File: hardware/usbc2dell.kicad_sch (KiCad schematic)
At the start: 20 parts, among them J1 USB_C_Receptacle_PowerOnly_6P, J2 DELL_Charger, Q1 Q_NMOS_GDS, Q2 Q_NPN_BEC, SW1 SW_DIP_x04, U1 ATtiny1616-M, U2 FUSB302BMPX, U3 L7805

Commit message: add caps
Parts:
- added C1, C3: 100n, Capacitor_SMD:C_0603_1608Metric, symbol Device:C
- added C2, C4: 1u, Capacitor_SMD:C_0603_1608Metric, symbol Device:C
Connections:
- net GND: now also C1.2, C2.2, C3.2, C4.2
- net VBUS: now also C1.1, C2.1
- net VCC: now also C3.1, C4.1
- net Vout: now reaches J2.3 (Pin_3), Q1.3 (S)

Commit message: prod?
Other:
- note added: "LED"
- note added: "caps"
- note added: "support / protection"
- company: (none) -> H3
- title: (none) -> USB Type-C to legacy Charging-Connector Adapter
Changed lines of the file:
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@@
 	(generator_version "9.0")
 	(paper "A4")
+	(title_block
+		(title "USB Type-C to legacy Charging-Connector Adapter")
+		(date "2025")
+		(rev "v0.1")
+		(company "H3")
+	)
 	(rectangle
 		(start 101.6 101.6)
@@
 		)
 	)
+	(text "caps"
+		(exclude_from_sim no)
+		(at 87.63 147.32 0)
+		(effects
+			(font
+				(size 1.27 1.27)
+			)
+			(justify right top)
+		)
+	)
 	(text "Software:\n- Negotiate PD profile up to 20V\n- Emulate DELLCHG EEPROM with values from PD profile\n- Enable power output"
 		(exclude_from_sim no)
@@
 		)
 	)
+	(text "LED"
+		(exclude_from_sim no)
+		(at 87.63 102.87 0)
+		(effects
+			(font
+				(size 1.27 1.27)
+			)
+			(justify right top)
+		)
+	)
+	(text "support / protection"
+		(exclude_from_sim no)
+		(at 189.23 102.87 0)
+		(effects
+			(font
+				(size 1.27 1.27)
+			)
+			(justify right top)
+		)
+	)

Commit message: parts sel
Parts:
- C1, C3: LCSC (none) -> C14663
- C2, C4: LCSC (none) -> C15849
- D1: value LED_RGB -> TC5050RGBF08-3CJH-AF53A; LCSC (none) -> C784540
- J1: value USB_C_Receptacle_PowerOnly_6P -> TYPE-C-31-M-17; LCSC (none) -> C283540
- Q1: value Q_NMOS_GDS -> MDD50N03D; LCSC (none) -> C5357578
- Q2: value Q_NPN_BEC -> MMBT5551; LCSC (none) -> C2145
- R1: value 10k -> 4k7; LCSC (none) -> C23162
- R2, R3, R4: LCSC (none) -> C23162
- R5: LCSC (none) -> C22775
- TP1, TP2, TP3: now left out of the parts list
- U2: LCSC (none) -> C442699
- U3: LCSC (none) -> C86206
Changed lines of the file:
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@@
+			)
+		)
+		(property "LCSC" "C442699"
+			(at 99.06 68.58 0)
+			(effects
+				(font
+					(size 1.27 1.27)
+				)
+				(hide yes)
 			)
 		)
@@
 			)
 		)
+		(property "LCSC" "C14663"
+			(at 57.15 158.75 0)
+			(effects
+				(font
+					(size 1.27 1.27)
+				)
+				(hide yes)
+			)
+		)
 		(pin "1"
 		)
@@
 		(unit 1)
 		(exclude_from_sim no)
-		(in_bom yes)
+		(in_bom no)
 		(on_board yes)
 		(dnp no)
@@
 			)
 		)
+		(property "LCSC" "C14663"
+			(at 31.75 158.75 0)
+			(effects
+				(font
+					(size 1.27 1.27)
+				)
+				(hide yes)
+			)
+		)
 		(pin "1"
 		)
@@
 			)
 		)
+		(property "LCSC" "C15849"
+			(at 69.85 158.75 0)
+			(effects
+				(font
+					(size 1.27 1.27)
+				)
+				(hide yes)
+			)
+		)
 		(pin "1"
 		)
@@
 			)
 		)
+		(property "LCSC" "C23162"
+			(at 35.56 114.3 90)
+			(effects
+				(font
+					(size 1.27 1.27)
+				)
+				(hide yes)
+			)
+		)
 		(pin "2"
 		)
@@
 		)
 		(property "Description" "Resistor"
+			(at 152.4 124.46 0)
+			(effects
+				(font
+					(size 1.27 1.27)
+				)
+				(hide yes)
+			)
+		)
+		(property "LCSC" "C22775"
 			(at 152.4 124.46 0)
 			(effects
@@
 			)
 		)
-		(property "Value" "USB_C_Receptacle_PowerOnly_6P"
+		(property "Value" "TYPE-C-31-M-17"
 			(at 148.59 64.7699 0)
 			(effects
@@
 			)
 		)
+		(property "LCSC" "C283540"
+			(at 137.16 63.5 0)
+			(effects
+				(font
+					(size 1.27 1.27)
+				)
+				(hide yes)
+			)
+		)
 		(pin "B9"
 		)
@@
 			)
 		)
+		(property "LCSC" "C23162"
+			(at 35.56 119.38 90)
+			(effects
+				(font
+					(size 1.27 1.27)
+				)
+				(hide yes)
+			)
+		)
 		(pin "2"
 		)
@@
 			)
 		)
-		(property "Value" "Q_NPN_BEC"
+		(property "Value" "MMBT5551"
 			(at 135.89 126.9999 0)
 			(effects
@@
 		)
 		(property "Description" "NPN transistor, base/emitter/collector"
+			(at 130.81 125.73 0)
+			(effects
+				(font
+					(size 1.27 1.27)
+				)
+				(hide yes)
+			)
+		)
+		(property "LCSC" "C2145"
 			(at 130.81 125.73 0)
 			(effects
@@
 			)
 		)
+		(property "LCSC" "C15849"
+			(at 44.45 158.75 0)
+			(effects
+				(font
+					(size 1.27 1.27)
+				)
+				(hide yes)
+			)
+		)
 		(pin "1"
 		)
@@
 			)
 		)
-		(property "Value" "LED_RGB"
+		(property "Value" "TC5050RGBF08-3CJH-AF53A"
 			(at 44.45 107.95 0)
 			(effects
@@
 			)
 		)
+		(property "LCSC" "C784540"
+			(at 44.45 119.38 0)
+			(effects
+				(font
+					(size 1.27 1.27)
+				)
+				(hide yes)
+			)
+		)
 		(pin "6"
 		)
@@
 			)
 		)
-		(property "Value" "Q_NMOS_GDS"
+		(property "Value" "MDD50N03D"
 			(at 130.81 34.29 90)
 			(effects
@@
 			)
 		)
+		(property "LCSC" "C5357578"
+			(at 130.81 40.64 90)
+			(effects
+				(font
+					(size 1.27 1.27)
+				)
+				(hide yes)
+			)
+		)
 		(pin "3"
 		)
@@
 			)
 		)
+		(property "LCSC" "C23162"
+			(at 35.56 124.46 90)
+			(effects
+				(font
+					(size 1.27 1.27)
+				)
+				(hide yes)
+			)
+		)
 		(pin "2"
 		)
@@
 		(unit 1)
 		(exclude_from_sim no)
-		(in_bom yes)
+		(in_bom no)
 		(on_board yes)
 		(dnp no)
@@
 			)
 		)
-		(property "Value" "10k"
+		(property "Value" "4k7"
 			(at 123.19 43.1799 0)
 			(effects
@@
 		)
 		(property "Description" "Resistor"
+			(at 120.65 41.91 0)
+			(effects
+				(font
+					(size 1.27 1.27)
+				)
+				(hide yes)
+			)
+		)
+		(property "LCSC" "C23162"
 			(at 120.65 41.91 0)
 			(effects
@@
 			)
 		)
+		(property "LCSC" "C86206"
+			(at 99.06 38.1 0)
+			(effects
+				(font
+					(size 1.27 1.27)
+				)
+				(hide yes)
+			)
+		)
 		(pin "1"
 		)
@@
 		(unit 1)
 		(exclude_from_sim no)
-		(in_bom yes)
-		(on_board yes)
-		(dnp no)
+		(in_bom no)
+		(on_board yes)
+		(dnp no)

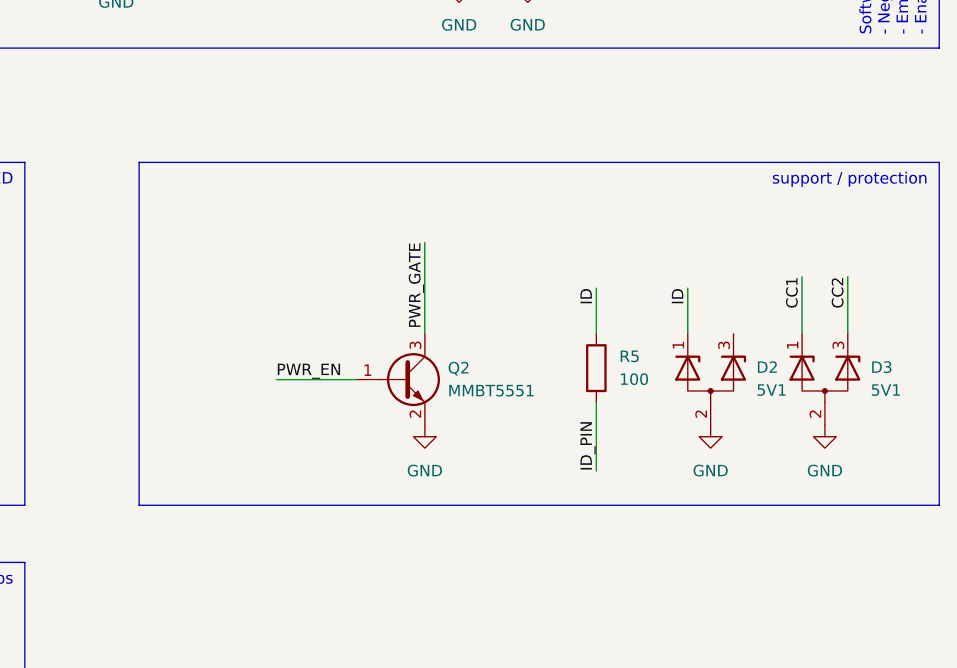
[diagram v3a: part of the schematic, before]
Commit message: change ESD diodes
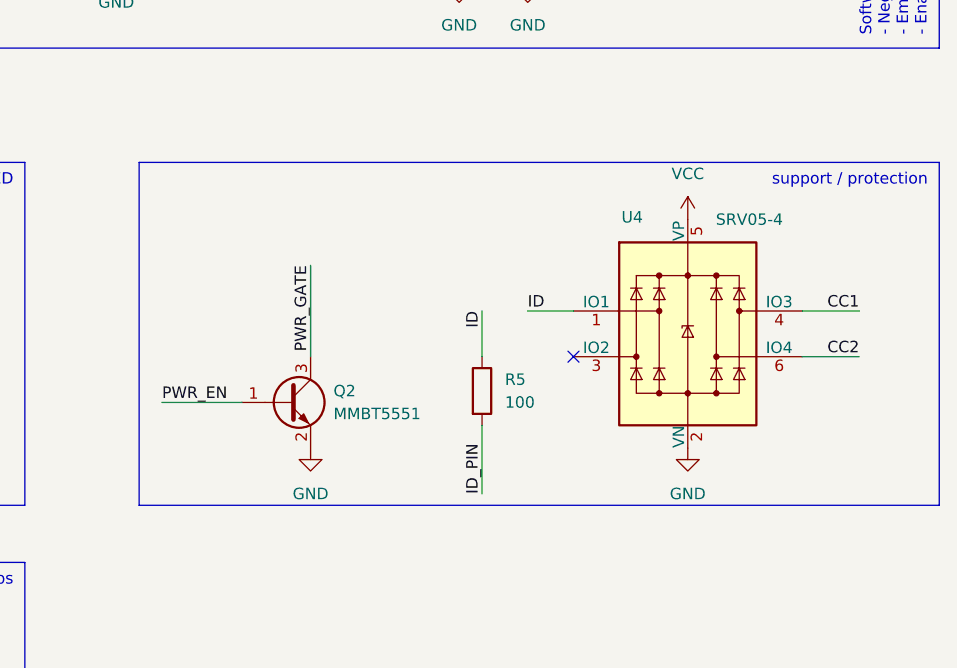
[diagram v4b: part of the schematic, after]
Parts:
- removed D2, D3: 5V1, Package_TO_SOT_SMD:SOT-23, symbol Device:D_Zener_Dual_CommonAnode_KAK_Parallel
- added U4: SRV05-4, Package_TO_SOT_SMD:SOT-23-6, symbol Power_Protection:SRV05-4
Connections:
- net CC1: now also U4.4 (IO3)
- net CC2: now also U4.6 (IO4)
- net GND: now also U4.2 (VN)
- net ID: now also U4.1 (IO1)
- net VCC: now also U4.5 (VP)
- no-connect marks 3 -> 4
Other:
- moved on the sheet: Q2, R5

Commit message: silk
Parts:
- U3: LCSC C86206 -> C54285
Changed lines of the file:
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@@
 			)
 		)
-		(property "LCSC" "C86206"
+		(property "LCSC" " C54285"
 			(at 99.06 38.1 0)
 			(effects

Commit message: partsel
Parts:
- SW1: value SW_DIP_x04 -> DSWB04LHGET; LCSC (none) -> C99418
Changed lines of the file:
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@@
 			)
 		)
-		(property "Value" "SW_DIP_x04"
+		(property "Value" "DSWB04LHGET"
 			(at 74.93 119.3799 90)
 			(effects
@@
 			(effects
 				(font
+					(size 1.27 1.27)
+				)
+				(hide yes)
+			)
+		)
+		(property "LCSC" "C99418"
+			(at 68.58 118.11 90)
+			(effects
+				(font

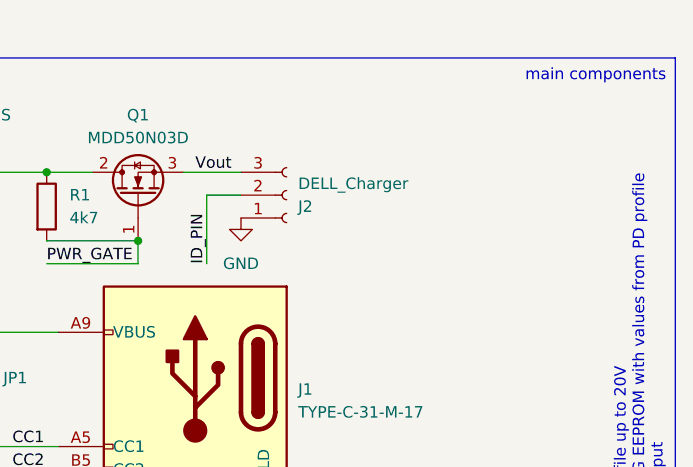
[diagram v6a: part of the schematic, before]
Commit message: switch to phoenix-style connectors
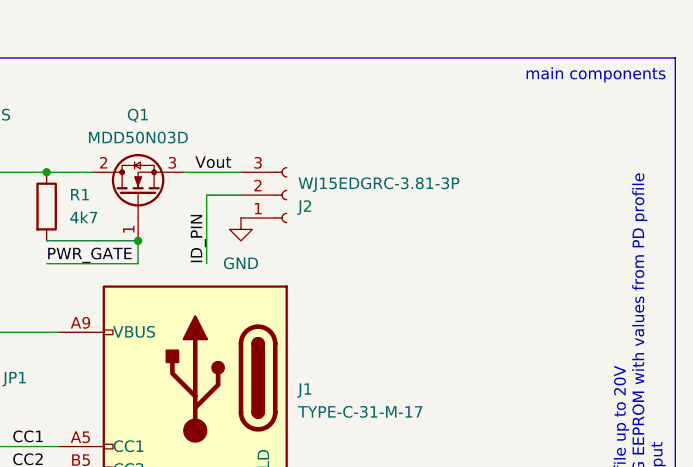
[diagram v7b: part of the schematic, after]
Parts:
- J2: value DELL_Charger -> WJ15EDGRC-3.81-3P; footprint TerminalBlock_WAGO:TerminalBlock_WAGO_236-103_1x03_P5.00mm_45Degree -> Connector_Phoenix_MC:PhoenixContact_MC_1,5_3-G-3.81_1x03_P3.81mm_Horizontal; LCSC (none) -> C8406
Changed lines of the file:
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@@
 			)
 		)
-		(property "Value" "DELL_Charger"
+		(property "Value" "WJ15EDGRC-3.81-3P"
 			(at 148.59 39.3701 0)
 			(effects
@@
 			)
 		)
-		(property "Footprint" "TerminalBlock_WAGO:TerminalBlock_WAGO_236-103_1x03_P5.00mm_45Degree"
+		(property "Footprint" "Connector_Phoenix_MC:PhoenixContact_MC_1,5_3-G-3.81_1x03_P3.81mm_Horizontal"
 			(at 147.32 40.64 0)
 			(effects
@@
 			(at 147.32 40.64 0)
 			(effects
+				(font
+					(size 1.27 1.27)
+				)
+				(hide yes)
+			)
+		)
+		(property "LCSC" "C8406"
+			(at 147.32 40.64 0)
+			(effects

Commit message: fix MOSFET
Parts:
- removed Q1: MDD50N03D, Package_TO_SOT_SMD:TO-252-3_TabPin2, symbol Transistor_FET:Q_NMOS_GDS
- added Q1: DOD50P06, Package_TO_SOT_SMD:TO-252-3_TabPin2, symbol Transistor_FET:Q_PMOS_GDS
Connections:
- net PWR_GATE: now also Q1.1 (G)
- net VBUS: now also Q1.3 (S)
- net Vout: now also Q1.2 (D)
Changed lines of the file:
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@@
-	)
-	(symbol
-		(lib_id "Transistor_FET:Q_NMOS_GDS")
-		(at 130.81 40.64 90)
-		(unit 1)
-		(exclude_from_sim no)
-		(in_bom yes)
-		(on_board yes)
-		(dnp no)
-		(fields_autoplaced yes)
-		(property "Reference" "Q1"
-			(at 130.81 31.75 90)
-			(effects
-				(font
-					(size 1.27 1.27)
-				)
-			)
-		)
-		(property "Value" "MDD50N03D"
-			(at 130.81 34.29 90)
-			(effects
-				(font
-					(size 1.27 1.27)
-				)
-			)
-		)
-		(property "Footprint" "Package_TO_SOT_SMD:TO-252-3_TabPin2"
-			(at 128.27 35.56 0)
-			(effects
-				(font
-					(size 1.27 1.27)
-				)
-				(hide yes)
-			)
-		)
-		(property "Datasheet" "~"
-			(at 130.81 40.64 0)
-			(effects
-				(font
-					(size 1.27 1.27)
-				)
-				(hide yes)
-			)
-		)
-		(property "Description" "N-MOSFET transistor, gate/drain/source"
-			(at 130.81 40.64 0)
-			(effects
-				(font
-					(size 1.27 1.27)
-				)
-				(hide yes)
-			)
-		)
-		(property "LCSC" "C5357578"
-			(at 130.81 40.64 90)
-			(effects
-				(font
-					(size 1.27 1.27)
-				)
-				(hide yes)
-			)
-		)
-		(pin "3"
-		)
-		(pin "2"
-		)
-		(pin "1"
-		)
-		(instances
-			(project ""
-				(path "/e67adff1-11e0-4c39-abac-ab102d4ad5db"
-					(reference "Q1")
-					(unit 1)
-				)
-			)
-		)
 	)
 	(symbol
@@
 					(unit 1)
 				)
+			)
+		)
+	)
+	(symbol
+		(lib_id "Transistor_FET:Q_PMOS_GDS")
+		(at 130.81 40.64 270)
+		(mirror x)
+		(unit 1)
+		(exclude_from_sim no)
+		(in_bom yes)
+		(on_board yes)
+		(dnp no)
+		(fields_autoplaced yes)
+		(property "Reference" "Q1"
+			(at 130.81 31.75 90)
+			(effects
+				(font
+					(size 1.27 1.27)
+				)
+			)
+		)
+		(property "Value" "DOD50P06"
+			(at 130.81 34.29 90)
+			(effects
+				(font
+					(size 1.27 1.27)
+				)
+			)
+		)
+		(property "Footprint" "Package_TO_SOT_SMD:TO-252-3_TabPin2"
+			(at 133.35 35.56 0)
+			(effects
+				(font
+					(size 1.27 1.27)
+				)
+				(hide yes)
+			)
+		)
+		(property "Datasheet" "~"
+			(at 130.81 40.64 0)
+			(effects
+				(font
+					(size 1.27 1.27)
+				)
+				(hide yes)
+			)
+		)
+		(property "Description" "P-MOSFET transistor, gate/drain/source"
+			(at 130.81 40.64 0)
+			(effects
+				(font
+					(size 1.27 1.27)
+				)
+				(hide yes)
+			)
+		)
+		(property "LCSC" "C41430590"
+			(at 130.81 40.64 90)
+			(effects
+				(font
+					(size 1.27 1.27)
+				)
+				(hide yes)
+			)
+		)
+		(pin "1"
+		)
+		(pin "3"
+		)
+		(pin "2"
+		)
+		(instances
+			(project ""
+				(path "/e67adff1-11e0-4c39-abac-ab102d4ad5db"
+					(reference "Q1")
+					(unit 1)
+				)
